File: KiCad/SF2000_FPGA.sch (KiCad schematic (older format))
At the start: 24 parts, among them J10 Conn_02x01, J11 Conn_02x01, J12 Conn_01x01, J3 Conn_02x03_Odd_Even, J4 Conn_02x01, J8 Conn_02x01, J9 Conn_02x01, U19 74LVC2G14, U28 GW1N-UV9LQ144, U8 T8Q144C3

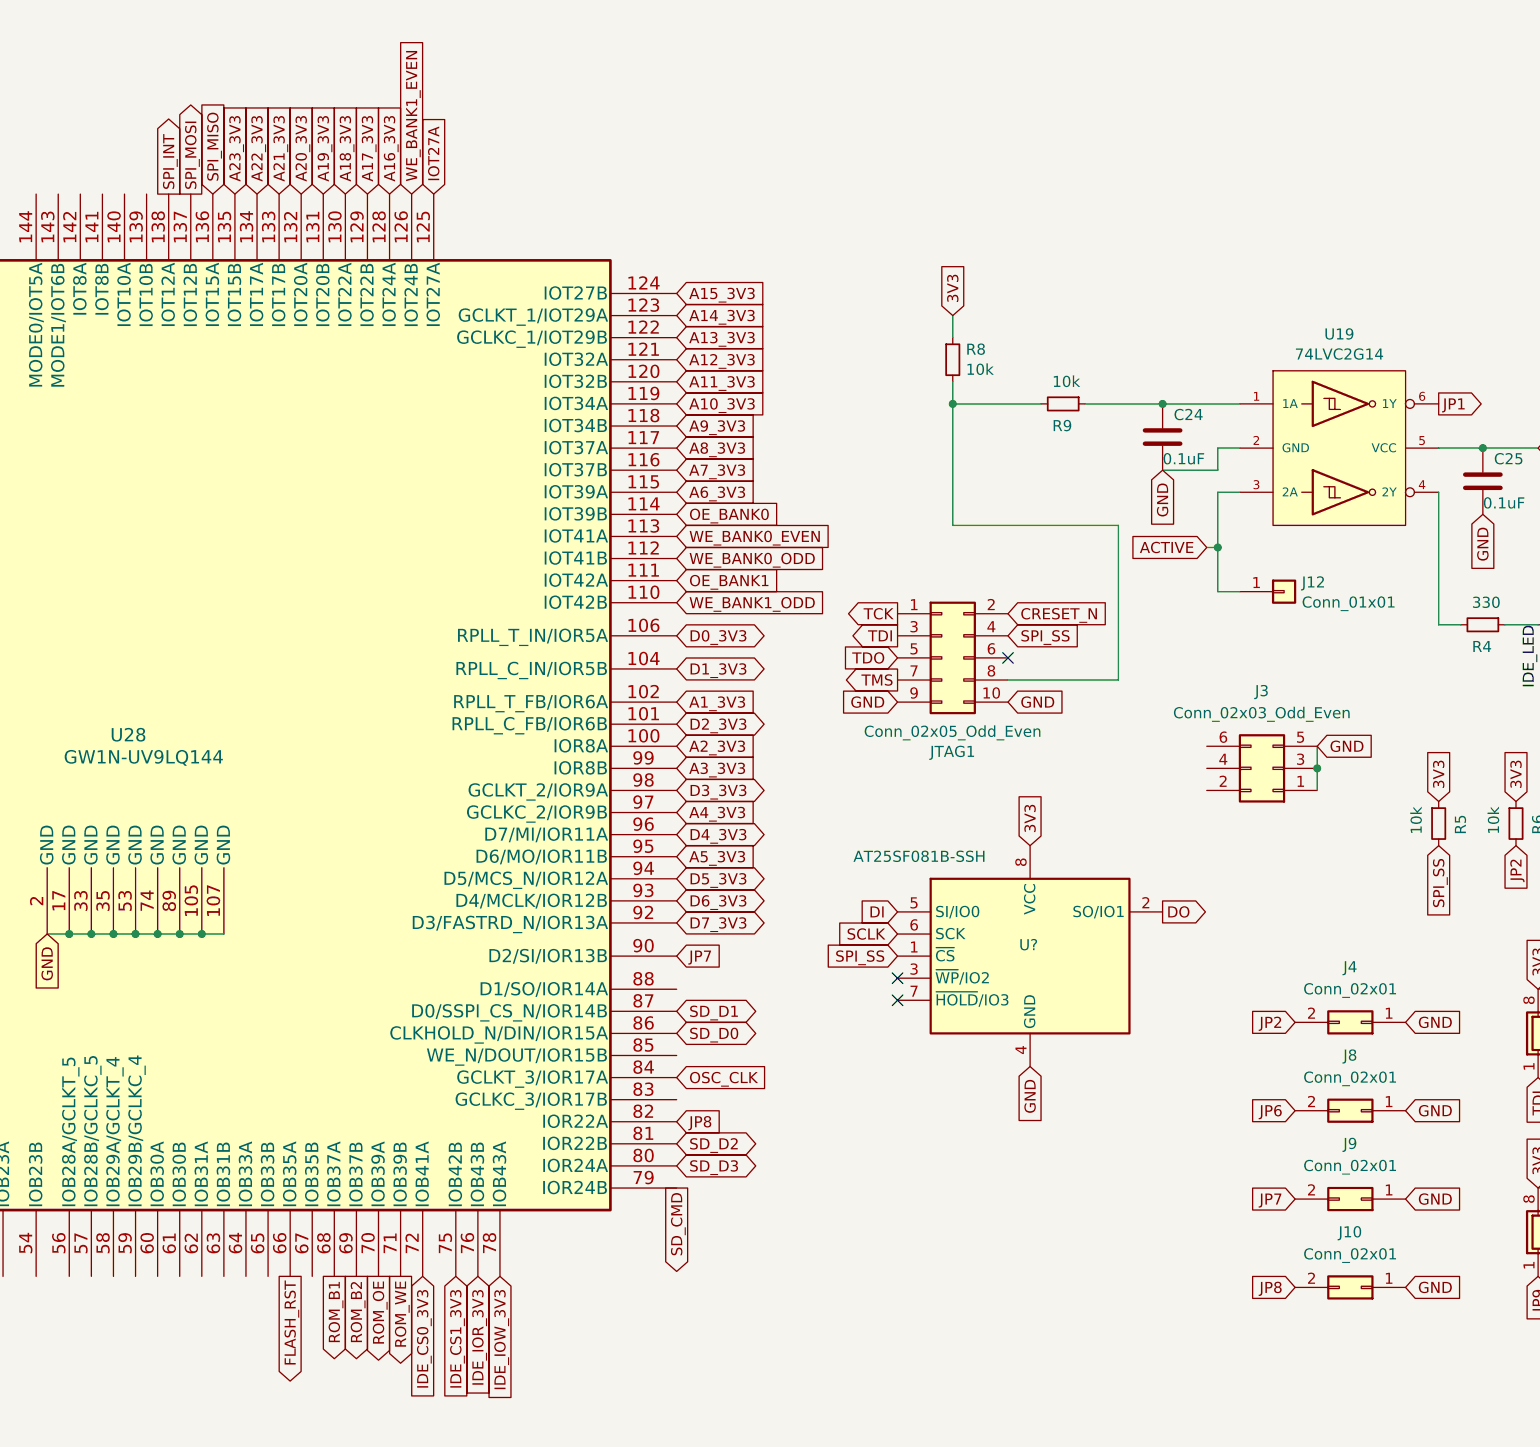
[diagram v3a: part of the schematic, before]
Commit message: Removed 3x2 jumper header J3, assigned JTAG header to now be J3 instead of JTAG1
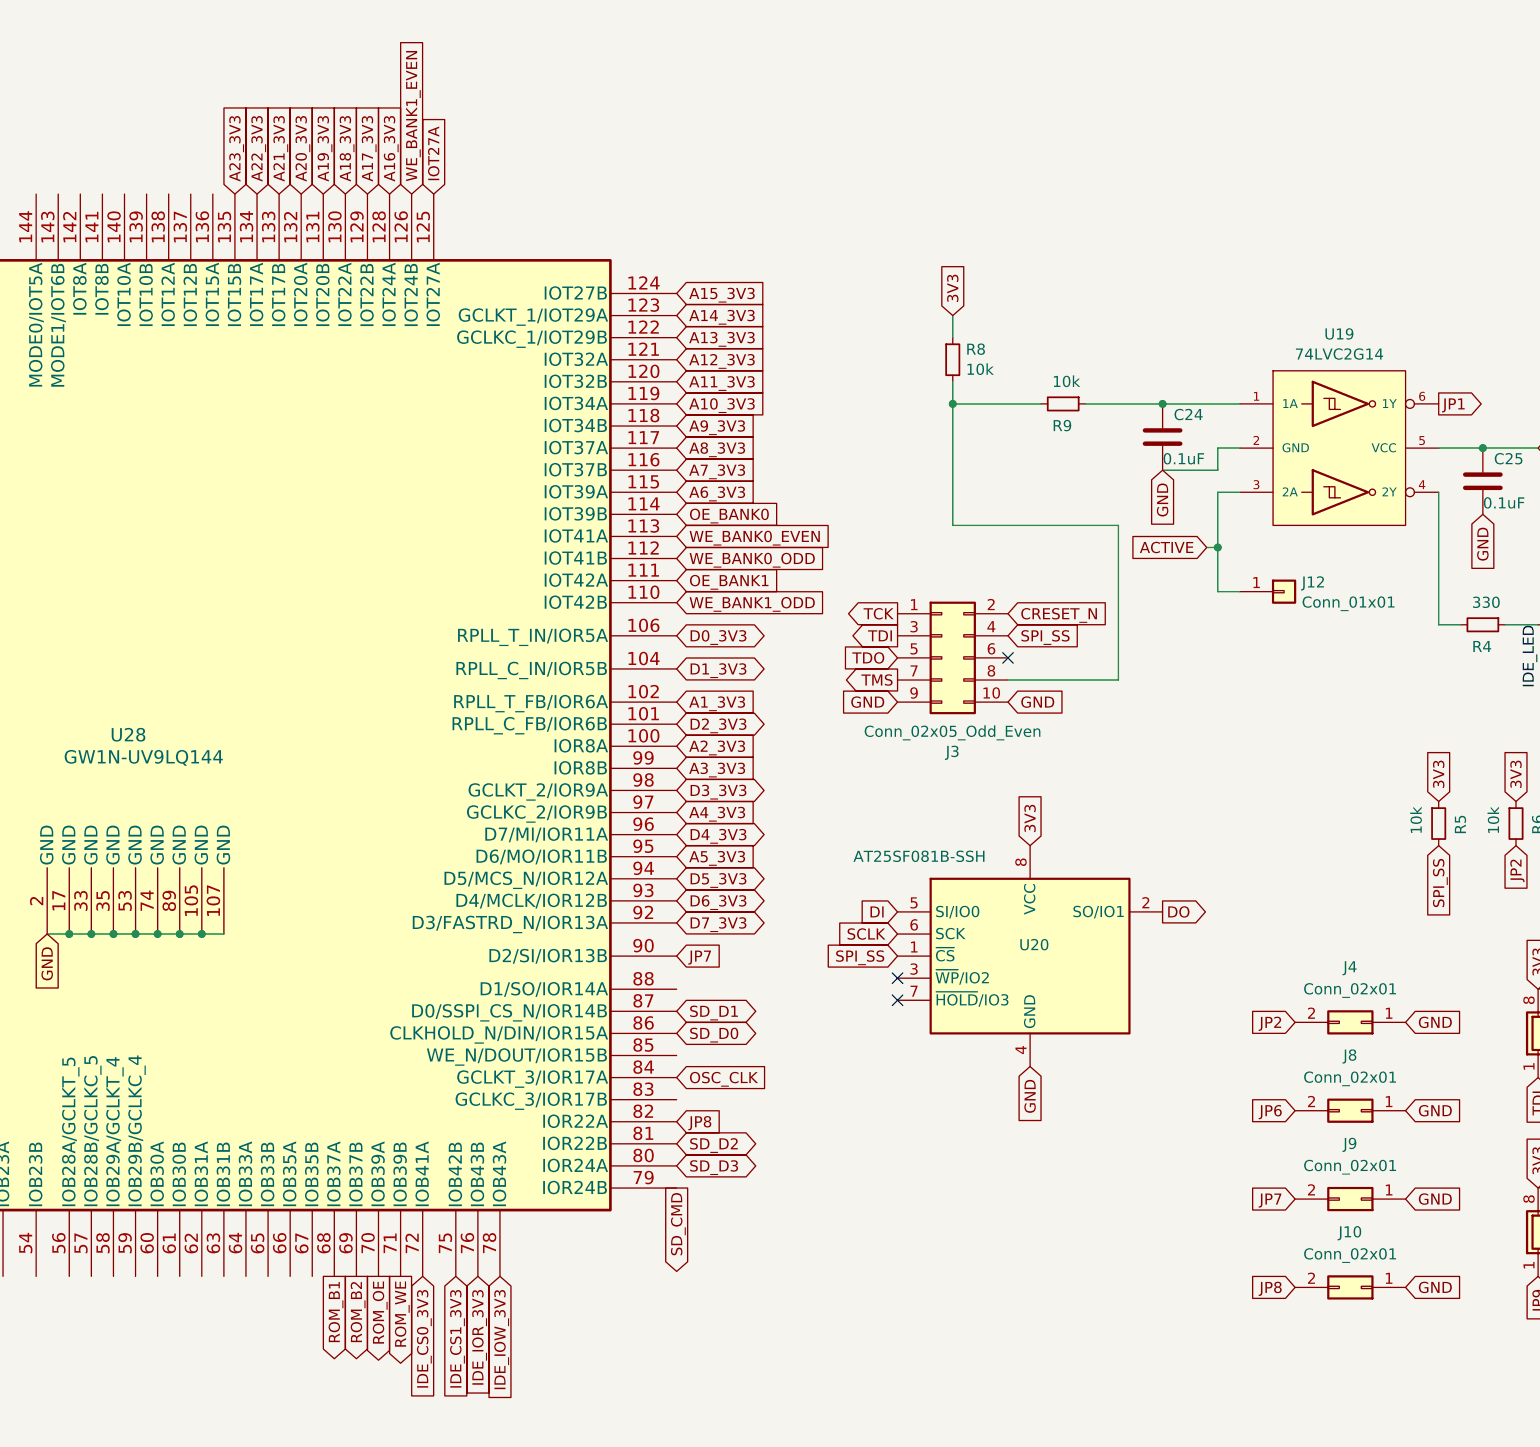
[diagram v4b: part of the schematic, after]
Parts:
- removed J3: Conn_02x03_Odd_Even, Connector_PinHeader_2.00mm:PinHeader_2x03_P2.00mm_Vertical, symbol Connector_Generic:Conn_02x03_Odd_Even
- gave numbers to parts that had none: 1
- renumbered JTAG1 to J3
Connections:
- net FLASH_RST: no longer names the net of U28.66 (IOB35A)
- net SPI_INT: no longer names the net of U28.138 (IOT12A)
- net SPI_MISO: no longer names the net of U28.136 (IOT15A)
- net SPI_MOSI: no longer names the net of U28.137 (IOT12B)
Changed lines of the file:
@@
 AS_MB_3V3
 $Comp
-L Connector_Generic:Conn_02x05_Odd_Even JTAG1
+L Connector_Generic:Conn_02x05_Odd_Even J3
 U 1 1 625BCAC6
 P 7450 3200
-F 0 "JTAG1" H 7500 2775 50  0000 C CNN
+F 0 "J3" H 7500 2775 50  0000 C CNN
 F 1 "Conn_02x05_Odd_Even" H 7500 2866 50  0000 C CNN
 F 2 "Connector_PinHeader_2.54mm:PinHeader_2x05_P2.54mm_Vertical" H 7450 3200 50  0001 C CNN
@@
 Text GLabel 7500 1650 1    50   Input ~ 0
 3V3
-$Comp
-L Connector_Generic:Conn_02x03_Odd_Even J3
-U 1 1 62704BD7
-P 8950 3700
-F 0 "J3" H 9000 3350 50  0000 C CNN
-F 1 "Conn_02x03_Odd_Even" H 9000 3450 50  0000 C CNN
-F 2 "Connector_PinHeader_2.00mm:PinHeader_2x03_P2.00mm_Vertical" H 8950 3700 50  0001 C CNN
-F 3 "~" H 8950 3700 50  0001 C CNN
-	1    8950 3700
-	-1   0    0    1
-$EndComp
-Wire Wire Line
-	9150 3600 9150 3700
-Connection ~ 9150 3700
-Wire Wire Line
-	9150 3700 9150 3800
-Text GLabel 9150 3600 2    50   Input ~ 0
-GND
 $Comp
 L Connector_Generic:Conn_02x01 J4
@@
 Text GLabel -900 5100 2    50   Output ~ 0
 FLASH_WE
-Text GLabel 4500 6000 3    50   Output ~ 0
-FLASH_RST
 Text GLabel 6250 4900 2    50   BiDi ~ 0
 SD_D0
@@
 Text GLabel 6250 1550 2    50   Input ~ 0
 A15_3V3
-Text GLabel 4150 1100 1    50   Input ~ 0
-SPI_MISO
-Text GLabel 4050 1100 1    50   Output ~ 0
-SPI_MOSI
 $Comp
 L Device:R_Small R?
@@
 Text GLabel 5150 1100 1    50   Input ~ 0
 IOT27A
-Text GLabel 3950 1100 1    50   Output ~ 0
-SPI_INT
 Text GLabel -6750 5000 0    50   Input ~ 0
 CDONE
@@
 $EndComp
 $Comp
-L Memory_Flash:AT25SF081-SSHD-X U?
+L Memory_Flash:AT25SF081-SSHD-X U20
 U 1 1 6925ADB2
 P 7850 4550
-F 0 "U?" H 7800 4600 50  0000 L CNN
+F 0 "U20" H 7800 4600 50  0000 L CNN
 F 1 "AT25SF081B-SSH" H 7050 5000 50  0000 L CNN
 F 2 "Package_SO:SOIC-8_3.9x4.9mm_P1.27mm" H 7850 3950 50  0001 C CNN

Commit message: Remove IDE ACTIVE signal and its LED-driver IC (74LVC2G14)
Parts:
- removed J12: Conn_01x01, Connector_PinHeader_2.54mm:PinHeader_1x01_P2.54mm_Vertical, symbol Connector_Generic:Conn_01x01
- removed U19: 74LVC2G14, Package_SO:TSOP-6_1.65x3.05mm_P0.95mm, symbol SF2000:74LVC2G14
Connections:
- net JP1: now also C24.1, R9.1
- net at R4.2: now also U8.75 (GPIOR_157_PLLIN)
- net ACTIVE: no longer names the net of R11.2
- net IDE_LED renamed SD_LED
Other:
- moved on the sheet: C24, C25, J11, J3, R3, R4, R8, R9, U20, U28, U8
